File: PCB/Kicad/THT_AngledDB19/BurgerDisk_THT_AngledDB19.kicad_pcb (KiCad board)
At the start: 2 copper layers, 93.7 x 73.4 mm, 17 parts, among them J1 Daisy port in, J2 MicroSD module, J3 UART, J4 Daisy port out, U1 PC817

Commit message: Modify holder a bit
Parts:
- added REF**: MountingHole_8.4mm_M8, MountingHole:MountingHole_8.4mm_M8, F.Cu at (157.0, 101.3)
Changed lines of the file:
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@@
     )
+  )
+  (footprint "MountingHole:MountingHole_8.4mm_M8" (layer "F.Cu")
+    (at 156.972 101.346)
+    (descr "Mounting Hole 8.4mm, no annular, M8")
+    (tags "mounting hole 8.4mm no annular m8")
+    (attr board_only exclude_from_pos_files exclude_from_bom)
+    (fp_text reference "REF**" (at 0 -9.4) (layer "F.Fab")
+        (effects (font (size 1 1) (thickness 0.15)))
+    )
+    (fp_text value "MountingHole_8.4mm_M8" (at 0 9.4) (layer "F.Fab")
+        (effects (font (size 1 1) (thickness 0.15)))
+    )
+    (fp_text user "${REFERENCE}" (at 0 0) (layer "F.Fab")
+        (effects (font (size 1 1) (thickness 0.15)))
+    )
+    (fp_circle (center 0 0) (end 8.4 0)
+      (stroke (width 0.15) (type solid)) (fill none) (layer "Cmts.User"))
+    (fp_circle (center 0 0) (end 8.65 0)
+      (stroke (width 0.05) (type solid)) (fill none) (layer "F.CrtYd"))
+    (pad "" np_thru_hole circle (at 0 0) (size 8.4 8.4) (drill 8.4) (layers "*.Cu" "*.Mask"))
   )
   (footprint "Resistor_THT:R_Axial_DIN0207_L6.3mm_D2.5mm_P7.62mm_Horizontal" (layer "F.Cu")

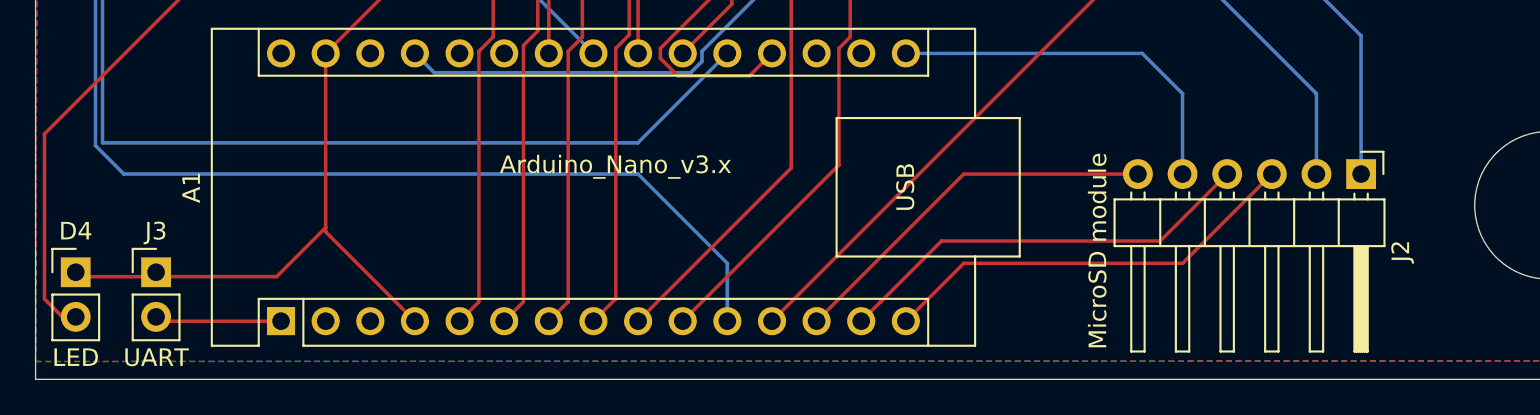
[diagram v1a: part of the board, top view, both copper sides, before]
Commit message: Add tooling to create JLCPCB BOM/CPL files
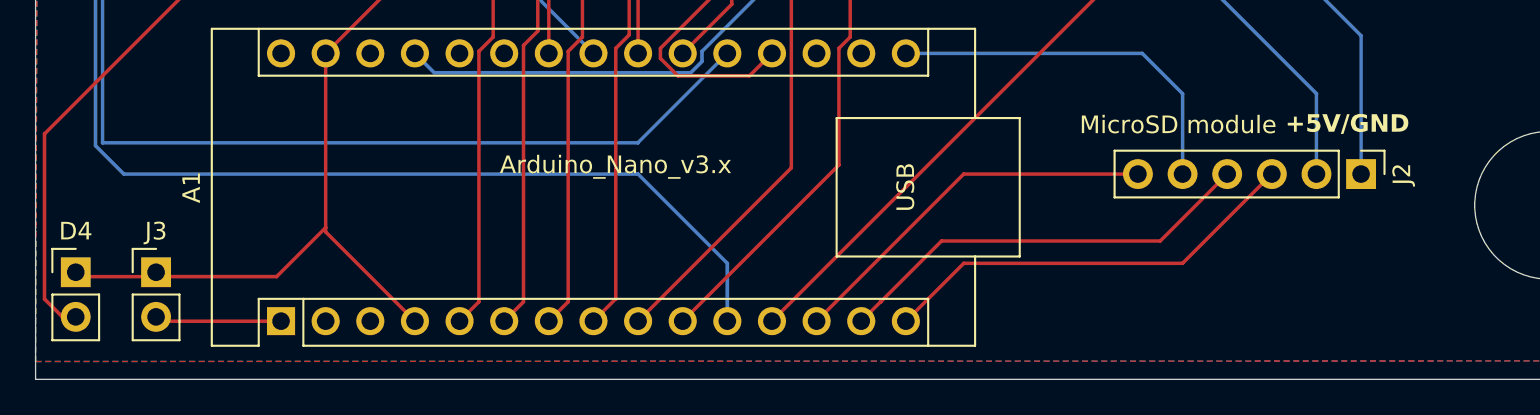
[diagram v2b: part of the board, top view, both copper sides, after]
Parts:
- J2: footprint Connector_PinHeader_2.54mm:PinHeader_1x06_P2.54mm_Horizontal -> Connector_PinHeader_2.54mm:PinHeader_1x06_P2.54mm_Vertical
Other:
- board text added: "+5V/GND"

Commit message: Small esthetic fixes
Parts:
- J2: footprint Connector_PinHeader_2.54mm:PinHeader_1x06_P2.54mm_Vertical -> Connector_PinHeader_2.54mm:PinHeader_1x06_P2.54mm_Horizontal
